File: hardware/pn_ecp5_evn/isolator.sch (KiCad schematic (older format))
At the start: 14 parts, among them U901 ADS7868, U902 ADS7868, U903 Si8640BB-B-IU, U904 Si8640BB-B-IU, U905 Si8642BB-B-IU

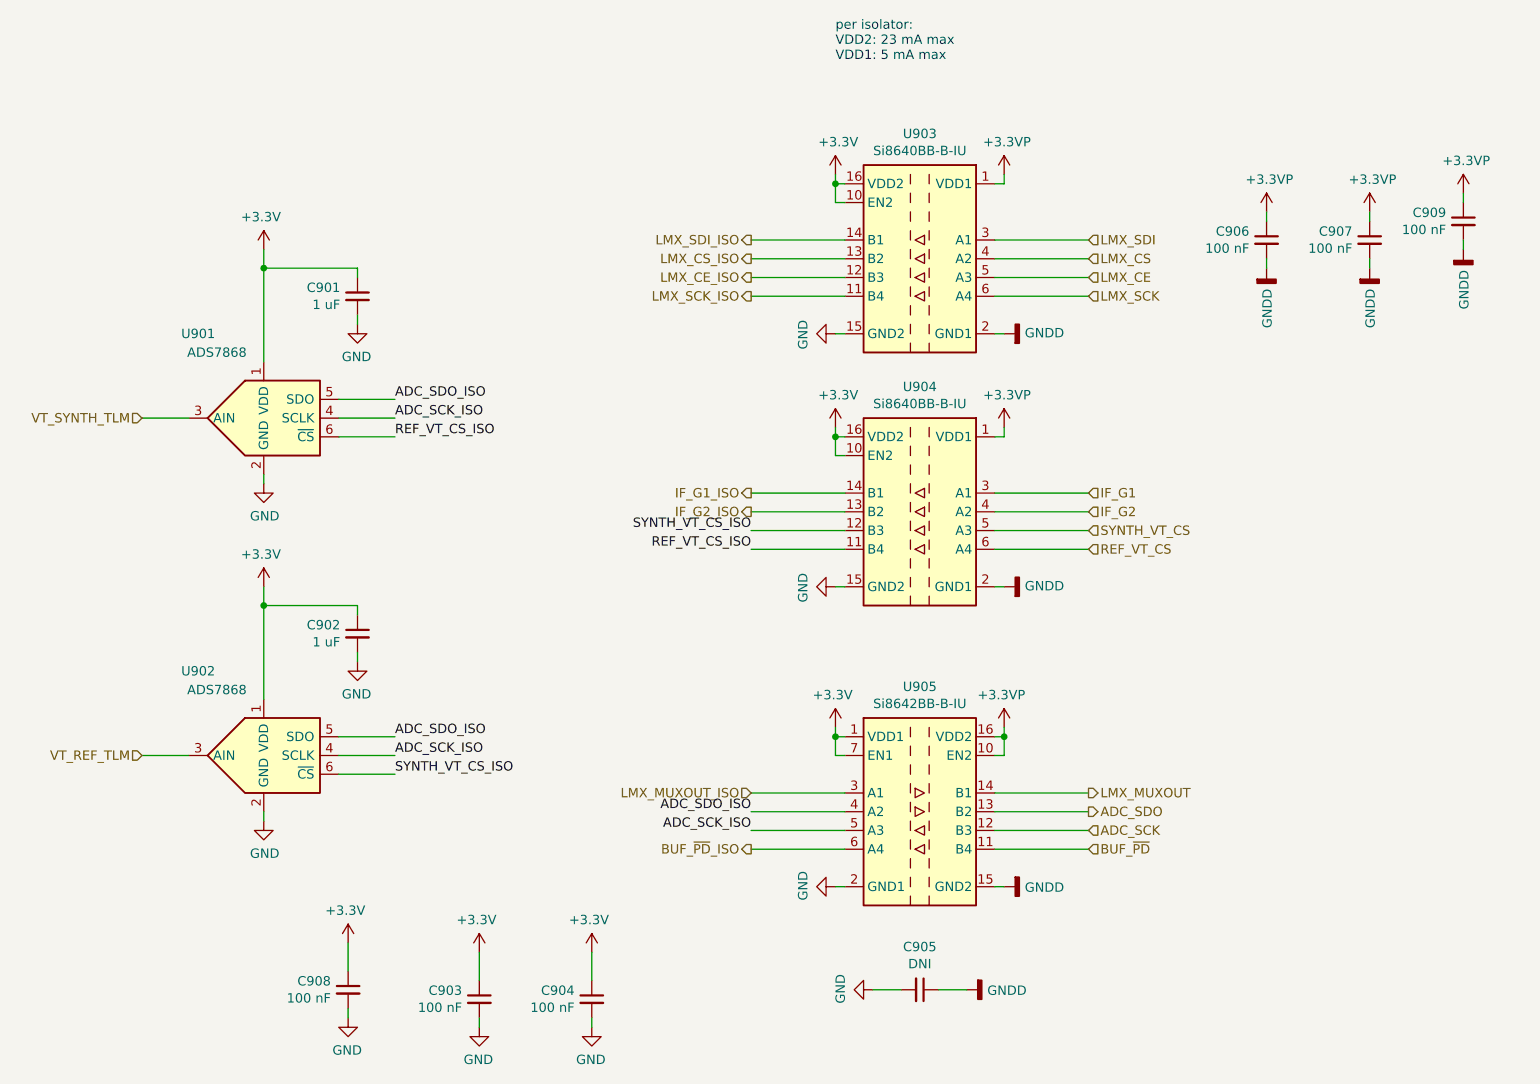
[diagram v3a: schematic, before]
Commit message: layout of phase noise downconverter
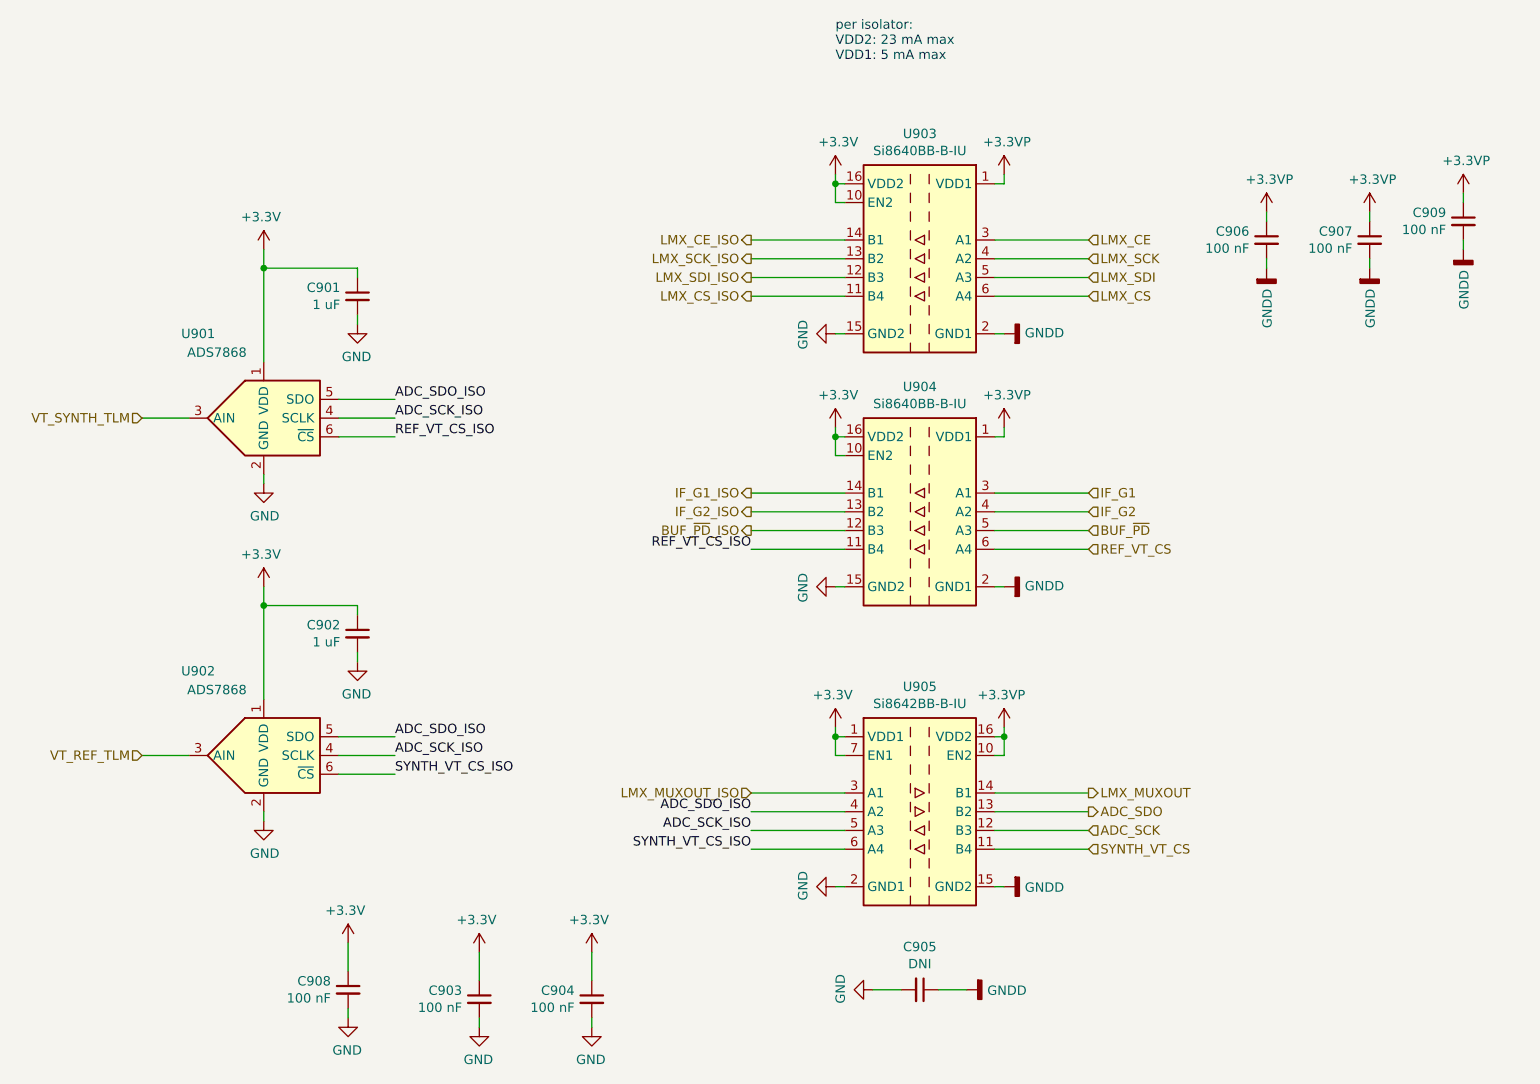
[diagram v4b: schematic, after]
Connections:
- net BUF_~PD: now also U904.5 (A3); no longer U905.11 (B4)
- net BUF_~PD~_ISO: now also U904.12 (B3); no longer U905.6 (A4)
- net LMX_CE: now also U903.3 (A1); no longer U903.5 (A3)
- net LMX_CE_ISO: now also U903.14 (B1); no longer U903.12 (B3)
- net LMX_CS: now also U903.6 (A4); no longer U903.4 (A2)
- net LMX_CS_ISO: now also U903.11 (B4); no longer U903.13 (B2)
- net LMX_SCK: now also U903.4 (A2); no longer U903.6 (A4)
- net LMX_SCK_ISO: now also U903.13 (B2); no longer U903.11 (B4)
- net LMX_SDI: now also U903.5 (A3); no longer U903.3 (A1)
- net LMX_SDI_ISO: now also U903.12 (B3); no longer U903.14 (B1)
- net SYNTH_VT_CS: now also U905.11 (B4); no longer U904.5 (A3)
- net SYNTH_VT_CS_ISO: now also U905.6 (A4); no longer U904.12 (B3)
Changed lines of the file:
@@
 Connection ~ 5050 1550
 Wire Wire Line
-	5900 2150 6400 2150
-Wire Wire Line
-	5900 2050 6400 2050
+	5900 1950 6400 1950
+Wire Wire Line
+	5900 1850 6400 1850
 Wire Wire Line
 	5900 3300 6400 3300
@@
 	5900 3200 6400 3200
 Wire Wire Line
-	4600 2050 5100 2050
+	4600 1850 5100 1850
 Wire Wire Line
 	4600 3300 5100 3300
@@
 	5900 3500 6400 3500
 Wire Wire Line
-	5900 3400 6400 3400
-Wire Wire Line
-	5900 1850 6400 1850
-Wire Wire Line
-	5900 1950 6400 1950
+	5900 2050 6400 2050
+Wire Wire Line
+	5900 2150 6400 2150
 Wire Wire Line
 	4600 3500 5100 3500
 Wire Wire Line
-	4600 3400 5100 3400
-Wire Wire Line
-	4600 1850 5100 1850
-Wire Wire Line
-	4600 1950 5100 1950
+	4600 2050 5100 2050
+Wire Wire Line
+	4600 2150 5100 2150
 Text HLabel 4600 3200 0    50   Output ~ 0
 IF_G1_ISO
 Text HLabel 4600 3300 0    50   Output ~ 0
 IF_G2_ISO
+Text HLabel 4600 1850 0    50   Output ~ 0
+LMX_CE_ISO
+Text HLabel 4600 1950 0    50   Output ~ 0
+LMX_SCK_ISO
+Text HLabel 4600 2150 0    50   Output ~ 0
+LMX_CS_ISO
 Text HLabel 4600 2050 0    50   Output ~ 0
-LMX_CE_ISO
-Text HLabel 4600 2150 0    50   Output ~ 0
-LMX_SCK_ISO
-Text HLabel 4600 1950 0    50   Output ~ 0
-LMX_CS_ISO
-Text HLabel 4600 1850 0    50   Output ~ 0
 LMX_SDI_ISO
 Text HLabel 6400 3200 2    50   Input ~ 0
@@
 Text HLabel 6400 3300 2    50   Input ~ 0
 IF_G2
+Text HLabel 6400 1850 2    50   Input ~ 0
+LMX_CE
+Text HLabel 6400 1950 2    50   Input ~ 0
+LMX_SCK
+Text HLabel 6400 2150 2    50   Input ~ 0
+LMX_CS
 Text HLabel 6400 2050 2    50   Input ~ 0
-LMX_CE
-Text HLabel 6400 2150 2    50   Input ~ 0
-LMX_SCK
-Text HLabel 6400 1950 2    50   Input ~ 0
-LMX_CS
-Text HLabel 6400 1850 2    50   Input ~ 0
 LMX_SDI
-Text HLabel 6400 3400 2    50   Input ~ 0
-SYNTH_VT_CS
 Text HLabel 6400 3500 2    50   Input ~ 0
 REF_VT_CS
-Text Label 4600 3400 2    50   ~ 0
-SYNTH_VT_CS_ISO
 Text Label 4600 3500 2    50   ~ 0
 REF_VT_CS_ISO
@@
 LMX_MUXOUT_ISO
 Wire Wire Line
-	4600 2150 5100 2150
+	4600 1950 5100 1950
 Text Label 4600 5000 2    50   ~ 0
 ADC_SCK_ISO
@@
 Wire Wire Line
 	3150 5650 3150 5800
-Text HLabel 6400 5100 2    50   Input ~ 0
-BUF_~PD
-Wire Wire Line
-	6400 5100 5900 5100
-Text HLabel 4600 5100 0    50   Output ~ 0
-BUF_~PD~_ISO
-Wire Wire Line
-	4600 5100 5100 5100
 Wire Wire Line
 	2450 5950 2450 6000
@@
 Wire Wire Line
 	8400 1650 8400 1600
+Text HLabel 6400 3400 2    50   Input ~ 0
+BUF_~PD
+Wire Wire Line
+	6400 3400 5900 3400
+Text HLabel 4600 3400 0    50   Output ~ 0
+BUF_~PD~_ISO
+Wire Wire Line
+	4600 3400 5100 3400
+Wire Wire Line
+	4600 5100 5100 5100
+Text Label 4600 5100 2    50   ~ 0
+SYNTH_VT_CS_ISO
+Wire Wire Line
+	5900 5100 6400 5100
+Text HLabel 6400 5100 2    50   Input ~ 0
+SYNTH_VT_CS
 $EndSCHEMATC

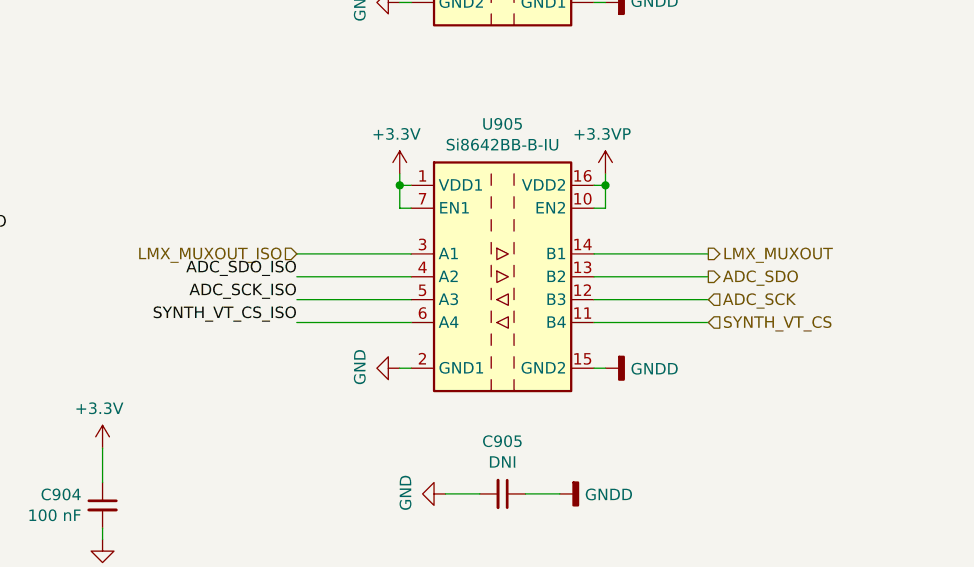
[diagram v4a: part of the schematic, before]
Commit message: all nets connected in layout
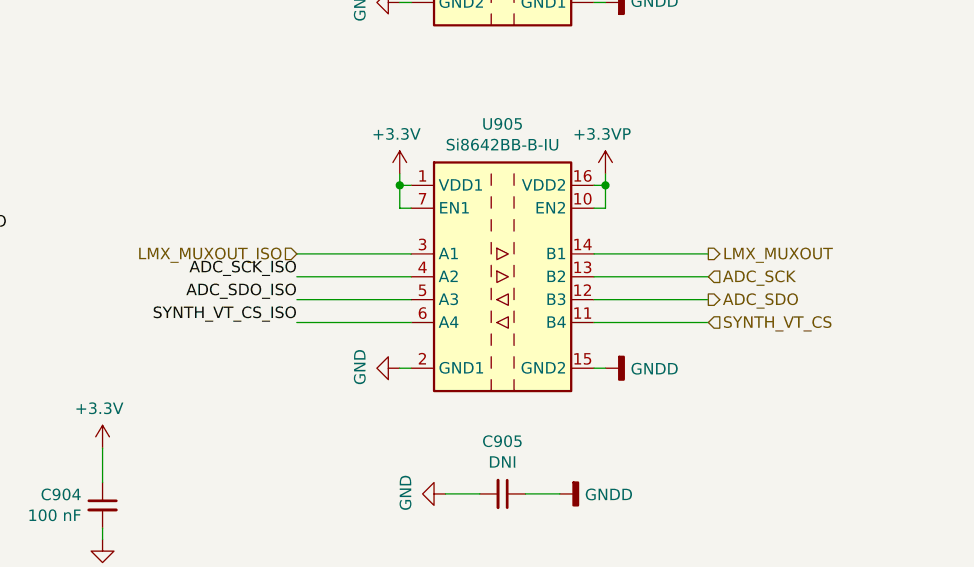
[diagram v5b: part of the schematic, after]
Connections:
- net ADC_SCK: now also U905.13 (B2); no longer U905.12 (B3)
- net ADC_SCK_ISO: now also U905.4 (A2); no longer U905.5 (A3)
- net ADC_SDO: now also U905.12 (B3); no longer U905.13 (B2)
- net ADC_SDO_ISO: now also U905.5 (A3); no longer U905.4 (A2)
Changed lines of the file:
@@
 Wire Wire Line
 	4600 1950 5100 1950
+Text Label 4600 4900 2    50   ~ 0
+ADC_SCK_ISO
 Text Label 4600 5000 2    50   ~ 0
-ADC_SCK_ISO
-Text Label 4600 4900 2    50   ~ 0
 ADC_SDO_ISO
 Wire Wire Line
@@
 	5100 4900 4600 4900
 Wire Wire Line
+	5900 5000 6400 5000
+Wire Wire Line
 	5900 4900 6400 4900
-Wire Wire Line
-	5900 5000 6400 5000
 Wire Wire Line
 	5900 4800 6400 4800
 Text HLabel 6400 4800 2    50   Output ~ 0
 LMX_MUXOUT
-Text HLabel 6400 5000 2    50   Input ~ 0
+Text HLabel 6400 4900 2    50   Input ~ 0
 ADC_SCK
-Text HLabel 6400 4900 2    50   Output ~ 0
+Text HLabel 6400 5000 2    50   Output ~ 0
 ADC_SDO
 $Comp
